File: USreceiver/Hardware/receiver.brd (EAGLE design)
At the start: 98.4 x 69.8 mm, 55 parts, among them U1 LMP7712MM, U2 LMP7712MM, U3 LMP7712MM, U4 LMP7712MM, U5 LM1117MP-3.3

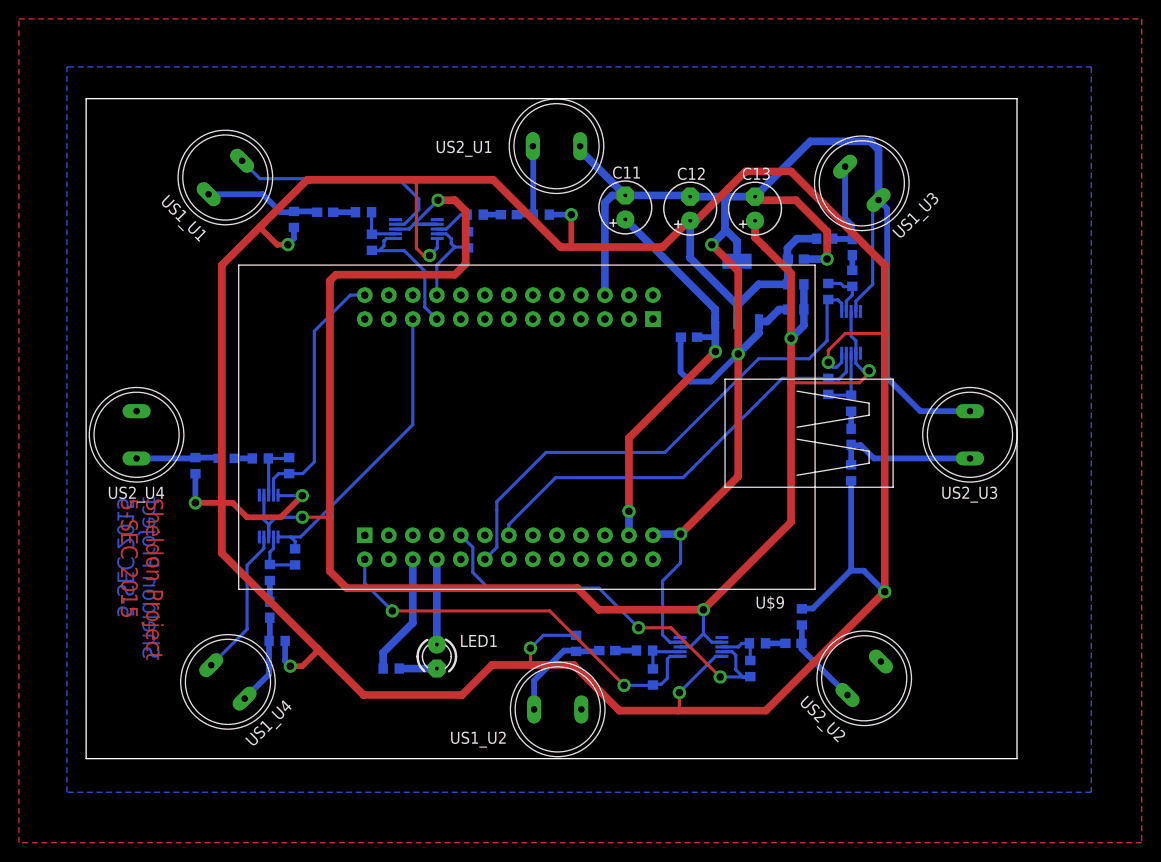
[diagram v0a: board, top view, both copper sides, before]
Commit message: Changed LMP7712 pad width because it was impossible to print the board
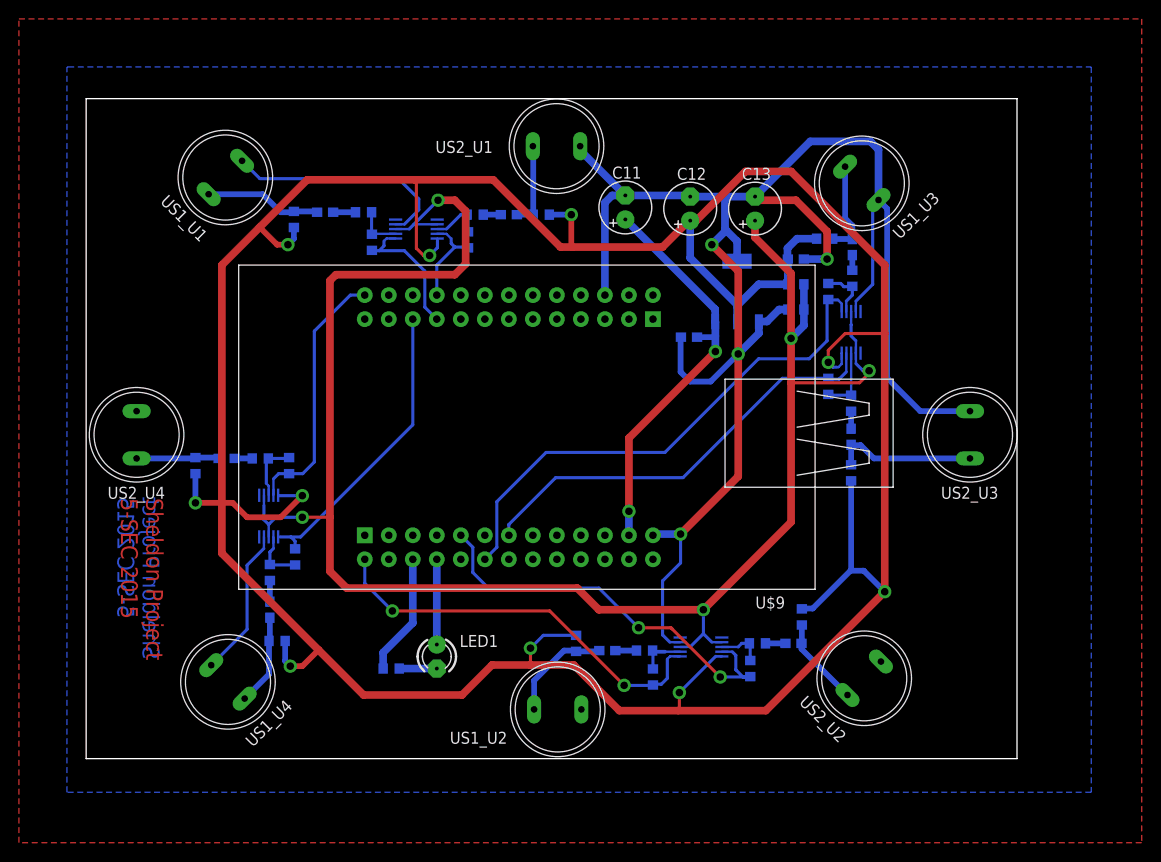
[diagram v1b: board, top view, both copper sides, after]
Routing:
- net VCC/2: track 196.6 -> 192.7 mm
